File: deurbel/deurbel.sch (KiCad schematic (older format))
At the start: 3 parts

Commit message: eerste commit
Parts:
- removed D?: D_Bridge_+-AA, symbol Device:D_Bridge_+-AA
- added BR?: DB107S, DIOB_DB107S, symbol DB107S:DB107S
- added BZ?: Buzzer, symbol Device:Buzzer
- added C?: CP, symbol Device:CP
- added D?: LED, symbol Device:LED
- added J?: Screw_Terminal_01x02, symbol Connector:Screw_Terminal_01x02
- added R?: R, symbol Device:R
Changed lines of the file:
@@
-$EndComp
-$Comp
-L Device:D_Bridge_+-AA D?
-U 1 1 5E266281
-P 4150 2200
-F 0 "D?" H 4494 2246 50  0000 L CNN
-F 1 "D_Bridge_+-AA" H 4494 2155 50  0000 L CNN
-F 2 "" H 4150 2200 50  0001 C CNN
-F 3 "~" H 4150 2200 50  0001 C CNN
-	1    4150 2200
-	1    0    0    -1
 $EndComp
 $Comp
@@
 	1    0    0    -1
 $EndComp
+$Comp
+L DB107S:DB107S BR?
+U 1 1 5E330B72
+P 4900 2650
+F 0 "BR?" H 5344 2696 30  0000 L CNN
+F 1 "DB107S" H 5344 2605 30  0000 L CNN
+F 2 "DIOB_DB107S" H 4900 2650 30  0001 L BNN
+F 3 "Rectron Semiconductor" H 4900 2650 50  0001 L BNN
+	1    4900 2650
+	1    0    0    -1
+$EndComp
+$Comp
+L Connector:Screw_Terminal_01x02 J?
+U 1 1 5E332FE3
+P 4200 1850
+F 0 "J?" H 4280 1842 50  0000 L CNN
+F 1 "Screw_Terminal_01x02" H 4280 1751 30  0000 L CNN
+F 2 "" H 4200 1850 50  0001 C CNN
+F 3 "~" H 4200 1850 50  0001 C CNN
+	1    4200 1850
+	1    0    0    -1
+$EndComp
+$Comp
+L Device:CP C?
+U 1 1 5E2A42C6
+P 3600 2600
+F 0 "C?" H 3718 2646 50  0000 L CNN
+F 1 "CP" H 3718 2555 50  0000 L CNN
+F 2 "" H 3638 2450 50  0001 C CNN
+F 3 "~" H 3600 2600 50  0001 C CNN
+	1    3600 2600
+	1    0    0    -1
+$EndComp
+$Comp
+L Device:Buzzer BZ?
+U 1 1 5E2A544C
+P 3400 3500
+F 0 "BZ?" H 3552 3529 50  0000 L CNN
+F 1 "Buzzer" H 3552 3438 50  0000 L CNN
+F 2 "" V 3375 3600 50  0001 C CNN
+F 3 "~" V 3375 3600 50  0001 C CNN
+	1    3400 3500
+	1    0    0    -1
+$EndComp
+$Comp
+L Device:LED D?
+U 1 1 5E2A6735
+P 1500 3000
+F 0 "D?" H 1493 3216 50  0000 C CNN
+F 1 "LED" H 1493 3125 50  0000 C CNN
+F 2 "" H 1500 3000 50  0001 C CNN
+F 3 "~" H 1500 3000 50  0001 C CNN
+	1    1500 3000
+	1    0    0    -1
+$EndComp
+$Comp
+L Device:R R?
+U 1 1 5E2A816C
+P 2050 3000
+F 0 "R?" V 2257 3000 50  0000 C CNN
+F 1 "R" V 2166 3000 50  0000 C CNN
+F 2 "" V 1980 3000 50  0001 C CNN
+F 3 "~" H 2050 3000 50  0001 C CNN
+	1    2050 3000
+	0    -1   -1   0
+$EndComp
 $EndSCHEMATC

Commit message: eerste commit
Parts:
- added U?: LM358, symbol Amplifier_Operational:LM358
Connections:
- net labels added: +5v, 16V-DC, AC1, AC2, GND
- wire segments 0 -> 9
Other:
- moved on the sheet: BR?, C?, J?, U?
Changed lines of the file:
@@
 encoding utf-8
 Sheet 1 1
-Title ""
+Title "Wemos D1 Mini deurbel"
 Date "2020-01-21"
-Rev ""
-Comp "Easylab4Kids"
+Rev "0.01"
+Comp "©2020 Easylab4kids.nl"
 Comment1 ""
 Comment2 ""
 Comment3 ""
-Comment4 ""
+Comment4 "Wisselstroom in, stepdown naar 5v"
 $EndDescr
 $Comp
@@
 L Regulator_Linear:LM7805_TO220 U?
 U 1 1 5E277305
-P 4350 3350
-F 0 "U?" H 4350 3592 50  0000 C CNN
-F 1 "LM7805_TO220" H 4350 3501 50  0000 C CNN
-F 2 "Package_TO_SOT_THT:TO-220-3_Vertical" H 4350 3575 50  0001 C CIN
-F 3 "http://www.fairchildsemi.com/ds/LM/LM7805.pdf" H 4350 3300 50  0001 C CNN
-	1    4350 3350
+P 6125 2525
+F 0 "U?" H 6125 2767 50  0000 C CNN
+F 1 "LM7805_TO220" H 6125 2676 50  0000 C CNN
+F 2 "Package_TO_SOT_THT:TO-220-3_Vertical" H 6125 2750 50  0001 C CIN
+F 3 "http://www.fairchildsemi.com/ds/LM/LM7805.pdf" H 6125 2475 50  0001 C CNN
+	1    6125 2525
 	1    0    0    -1
 $EndComp
@@
 L DB107S:DB107S BR?
 U 1 1 5E330B72
-P 4900 2650
-F 0 "BR?" H 5344 2696 30  0000 L CNN
-F 1 "DB107S" H 5344 2605 30  0000 L CNN
-F 2 "DIOB_DB107S" H 4900 2650 30  0001 L BNN
-F 3 "Rectron Semiconductor" H 4900 2650 50  0001 L BNN
-	1    4900 2650
+P 4350 2525
+F 0 "BR?" H 4794 2571 30  0000 L CNN
+F 1 "DB107S" H 4794 2480 30  0000 L CNN
+F 2 "DIOB_DB107S" H 4350 2525 30  0001 L BNN
+F 3 "Rectron Semiconductor" H 4350 2525 50  0001 L BNN
+	1    4350 2525
 	1    0    0    -1
 $EndComp
@@
 L Connector:Screw_Terminal_01x02 J?
 U 1 1 5E332FE3
-P 4200 1850
-F 0 "J?" H 4280 1842 50  0000 L CNN
-F 1 "Screw_Terminal_01x02" H 4280 1751 30  0000 L CNN
-F 2 "" H 4200 1850 50  0001 C CNN
-F 3 "~" H 4200 1850 50  0001 C CNN
-	1    4200 1850
-	1    0    0    -1
+P 4250 1725
+F 0 "J?" V 4350 1675 50  0000 L CNN
+F 1 "Screw_Terminal_01x02" V 4450 1425 30  0000 L CNN
+F 2 "" H 4250 1725 50  0001 C CNN
+F 3 "~" H 4250 1725 50  0001 C CNN
+	1    4250 1725
+	0    -1   -1   0
 $EndComp
 $Comp
 L Device:CP C?
 U 1 1 5E2A42C6
-P 3600 2600
-F 0 "C?" H 3718 2646 50  0000 L CNN
-F 1 "CP" H 3718 2555 50  0000 L CNN
-F 2 "" H 3638 2450 50  0001 C CNN
-F 3 "~" H 3600 2600 50  0001 C CNN
-	1    3600 2600
-	1    0    0    -1
+P 5350 2525
+F 0 "C?" H 5468 2571 50  0000 L CNN
+F 1 "CP" H 5468 2480 50  0000 L CNN
+F 2 "" H 5388 2375 50  0001 C CNN
+F 3 "~" H 5350 2525 50  0001 C CNN
+	1    5350 2525
+	0    -1   -1   0
 $EndComp
 $Comp
@@
 	0    -1   -1   0
 $EndComp
+Wire Wire Line
+	4250 1925 4250 2125
+Wire Wire Line
+	4350 1925 4350 2125
+Text Label 4250 2075 1    34   ~ 0
+AC1
+Text Label 4350 2075 1    34   ~ 0
+AC2
+Wire Wire Line
+	4350 2925 4350 3250
+Text Label 4350 3200 1    34   ~ 0
+AC1
+Wire Wire Line
+	4750 2525 5200 2525
+Wire Wire Line
+	3950 2525 3725 2525
+Text Label 3825 2525 0    40   ~ 0
+GND
+Wire Wire Line
+	6125 2825 6125 3200
+Text Label 6125 3125 1    40   ~ 0
+GND
+Text Label 4950 2525 0    40   ~ 0
+16V-DC
+Wire Wire Line
+	5500 2525 5825 2525
+Text Label 6600 2525 0    40   ~ 0
++5v
+Wire Wire Line
+	6425 2525 6850 2525
+Wire Wire Line
+	2700 1600 2700 1300
+Text Label 2700 1425 3    40   ~ 0
++5v
+$Comp
+L Amplifier_Operational:LM358 U?
+U 1 1 5E2C42CD
+P 1875 4025
+F 0 "U?" H 1875 4392 50  0000 C CNN
+F 1 "LM358" H 1875 4301 50  0000 C CNN
+F 2 "" H 1875 4025 50  0001 C CNN
+F 3 "http://www.ti.com/lit/ds/symlink/lm2904-n.pdf" H 1875 4025 50  0001 C CNN
+	1    1875 4025
+	1    0    0    -1
+$EndComp
 $EndSCHEMATC

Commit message: eerste commit
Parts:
- added C?: CAP, symbol pspice:CAP
- added D?: DIODE, symbol pspice:DIODE
- added Q?: BC547, Package_TO_SOT_THT:TO-92_Inline, symbol Transistor_BJT:BC547
- added R?: 10k, symbol Device:R
- added R?: 5k, symbol Device:R
- added SW?: SW_Push, symbol Switch:SW_Push
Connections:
- net labels added: Buzzer, D0, D2, RST
- wire segments 9 -> 35
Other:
- note added: "esp8266-deep-sleep-mode-test-wake-pir-motion-detector"
- moved on the sheet: BR?, BZ?, C?, J?, U?

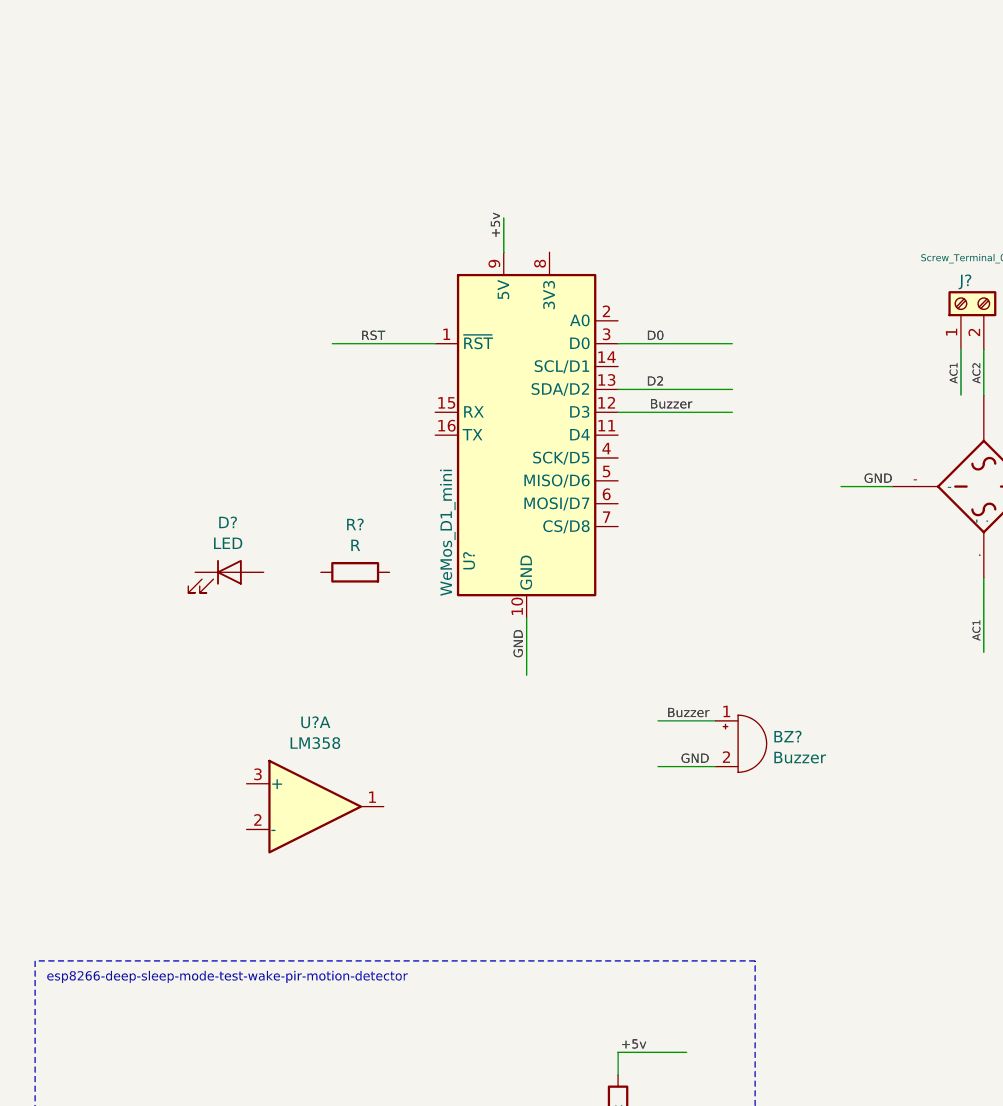
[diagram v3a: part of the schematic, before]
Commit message: LM358 opamp toevoeging werk-in-uitvoering
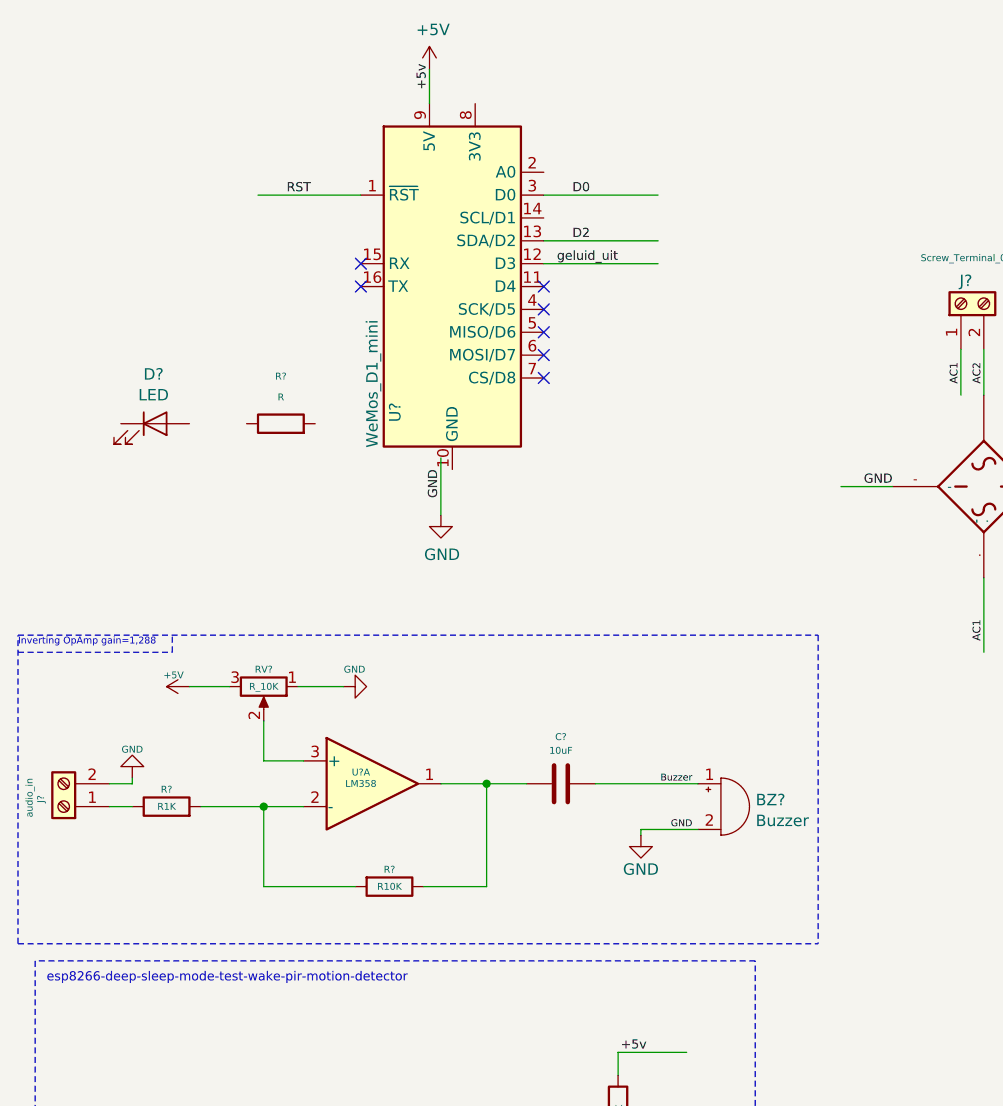
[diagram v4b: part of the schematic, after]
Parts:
- added C?: 10uF, symbol Device:C
- added J?: audio_in, symbol Connector:Screw_Terminal_01x02
- added R?: R10K, symbol Device:R
- added R?: R1K, symbol Device:R
- added RV?: R_10K, symbol Device:R_POT
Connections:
- net labels added: +5V, geluid_uit
- wire segments 35 -> 51
- no-connect marks 0 -> 7
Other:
- note added: "Inverting OpAmp gain=1,288"
- moved on the sheet: BZ?, D?, R?, U?, U?A

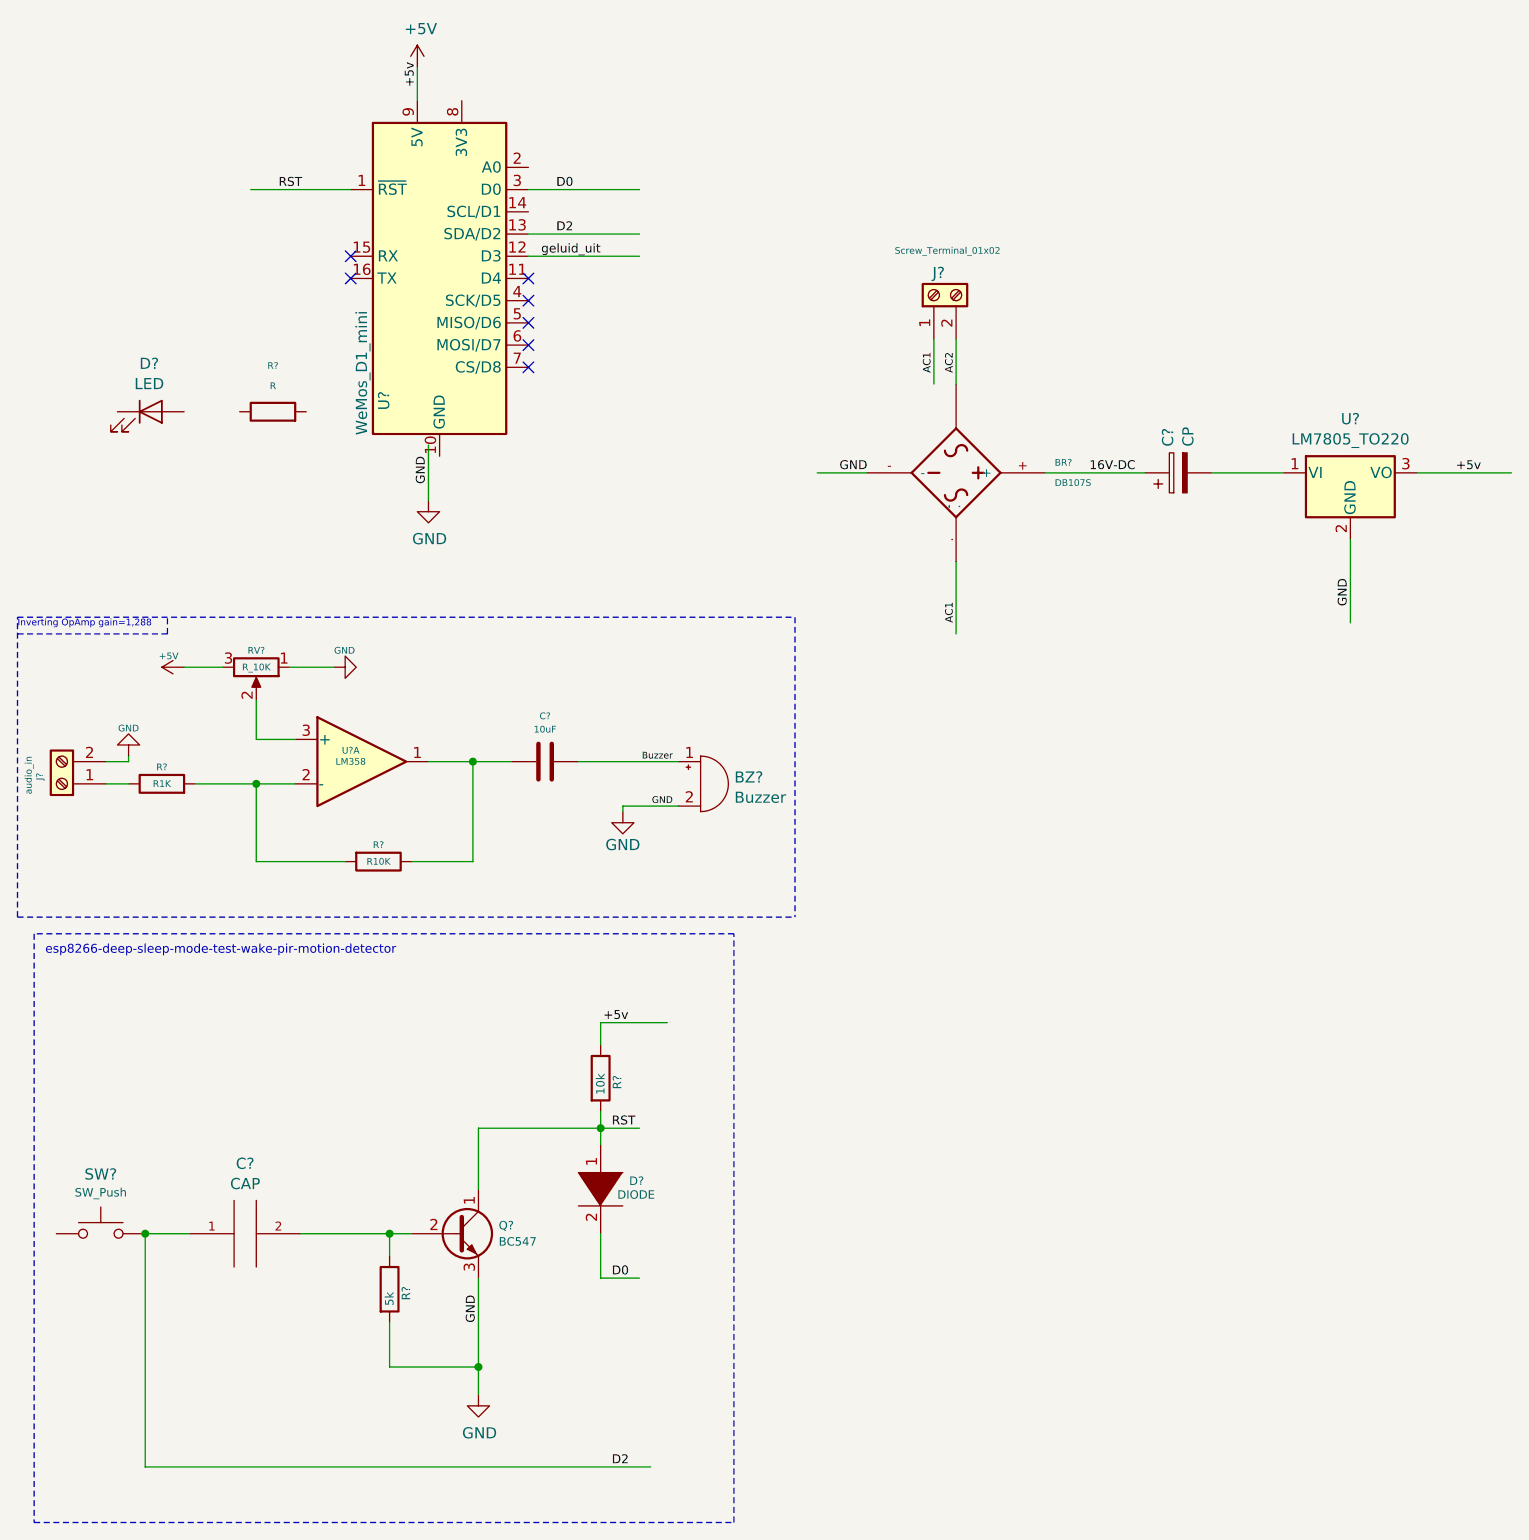
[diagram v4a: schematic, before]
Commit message: basislogic schema met circuitjs
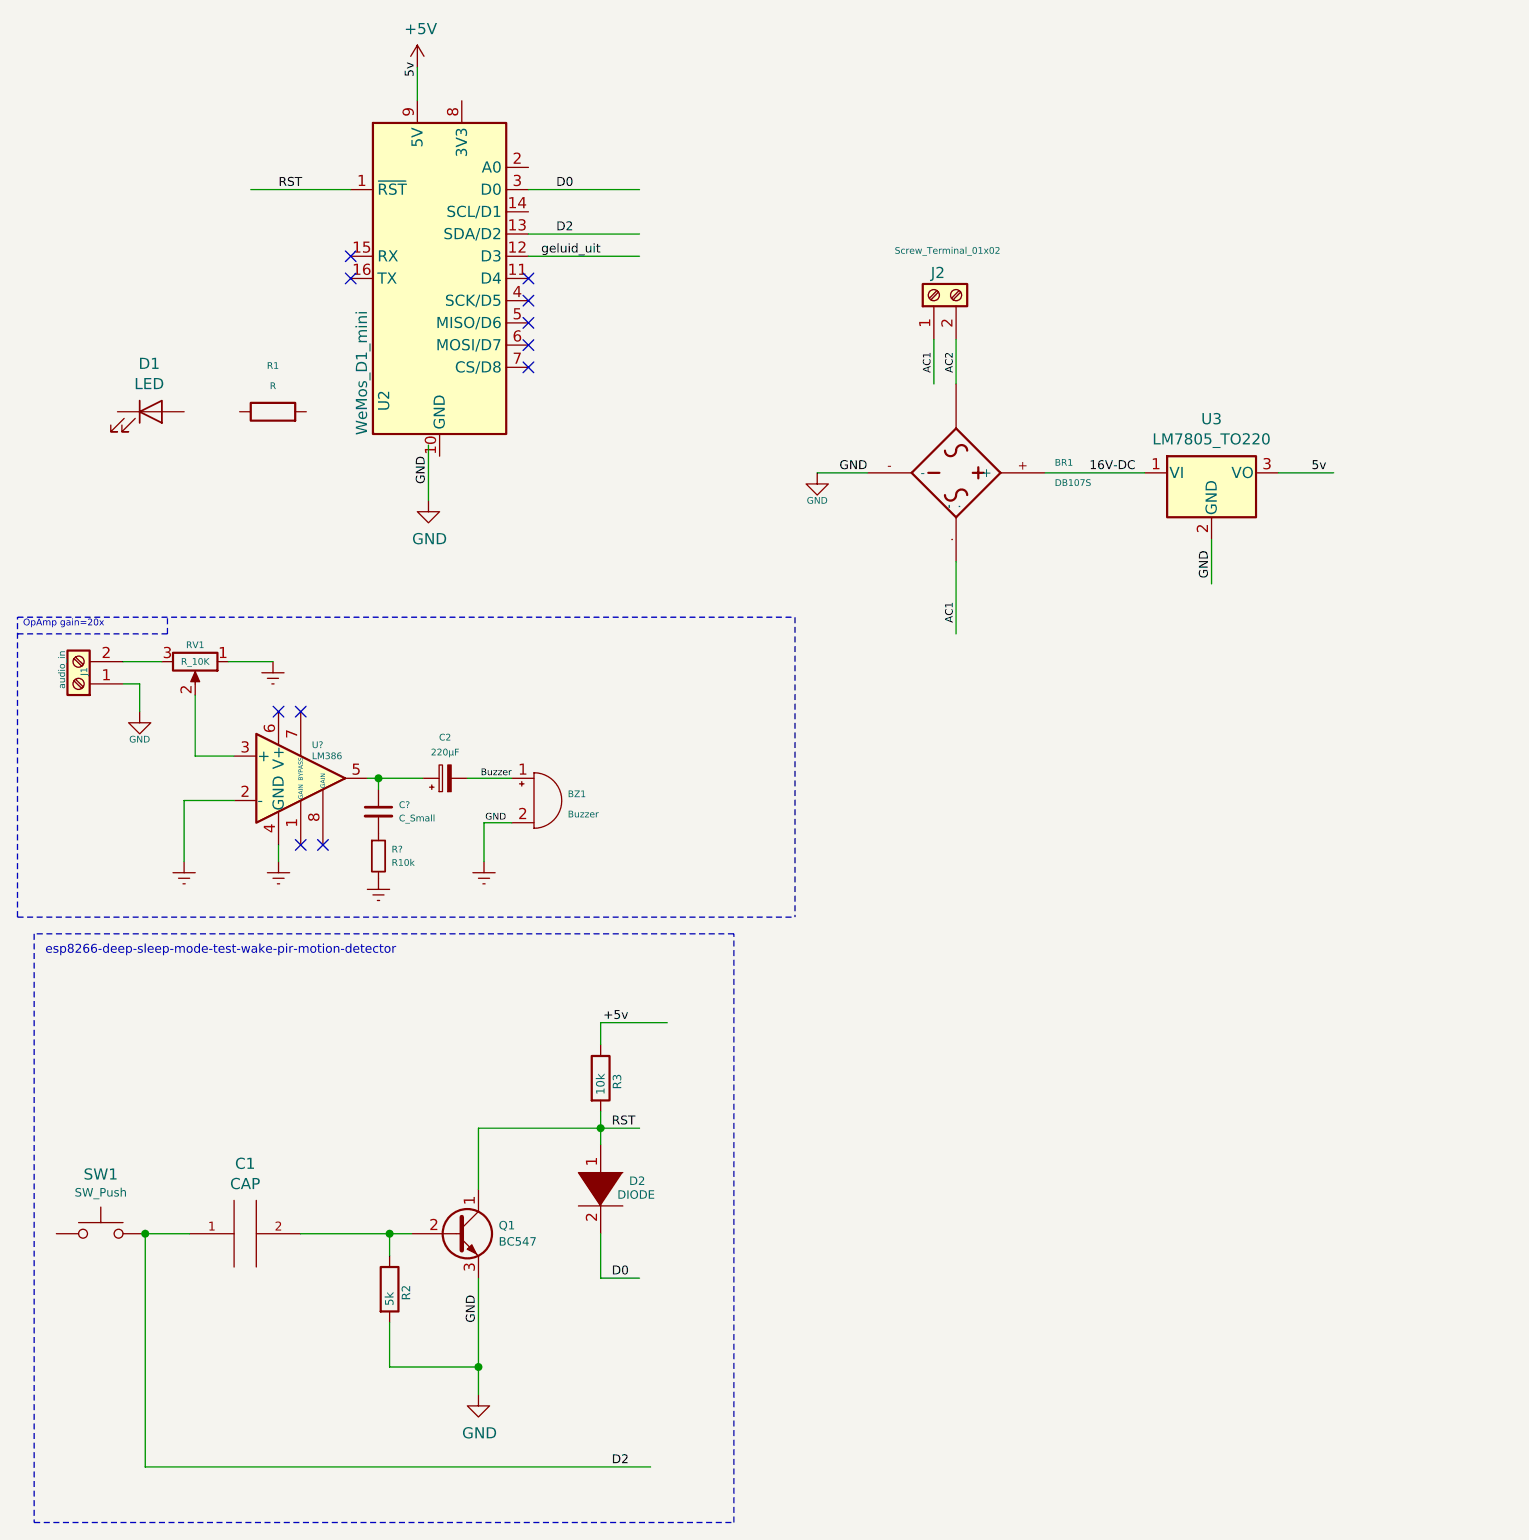
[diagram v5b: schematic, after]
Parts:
- removed C?: CP, symbol Device:CP
- removed C?: 10uF, symbol Device:C
- removed R?: R10K, symbol Device:R
- removed R?: R1K, symbol Device:R
- removed U?: LM358, symbol Amplifier_Operational:LM358
- added C2: 220µF, symbol Device:CP_Small
- added C?: C_Small, symbol Device:C_Small
- added R?: R10k, symbol Device:R_Small
- added U?: LM386, symbol Amplifier_Audio:LM386
- gave numbers to parts that had none: 15
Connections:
- net labels added: 5v, Earth
- wire segments 51 -> 47
- no-connect marks 7 -> 11
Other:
- note added: "OpAmp gain=20x"
- note removed: "Inverting OpAmp gain=1,288"
- moved on the sheet: BZ1, J1, RV1, U3
